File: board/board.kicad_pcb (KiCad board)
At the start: 2 copper layers, 93 x 29 mm, 5 parts, among them J1 022_battery_cells, J2 022_battery_cells, U1 BK-6223-TR, U2 BK-6223-TR

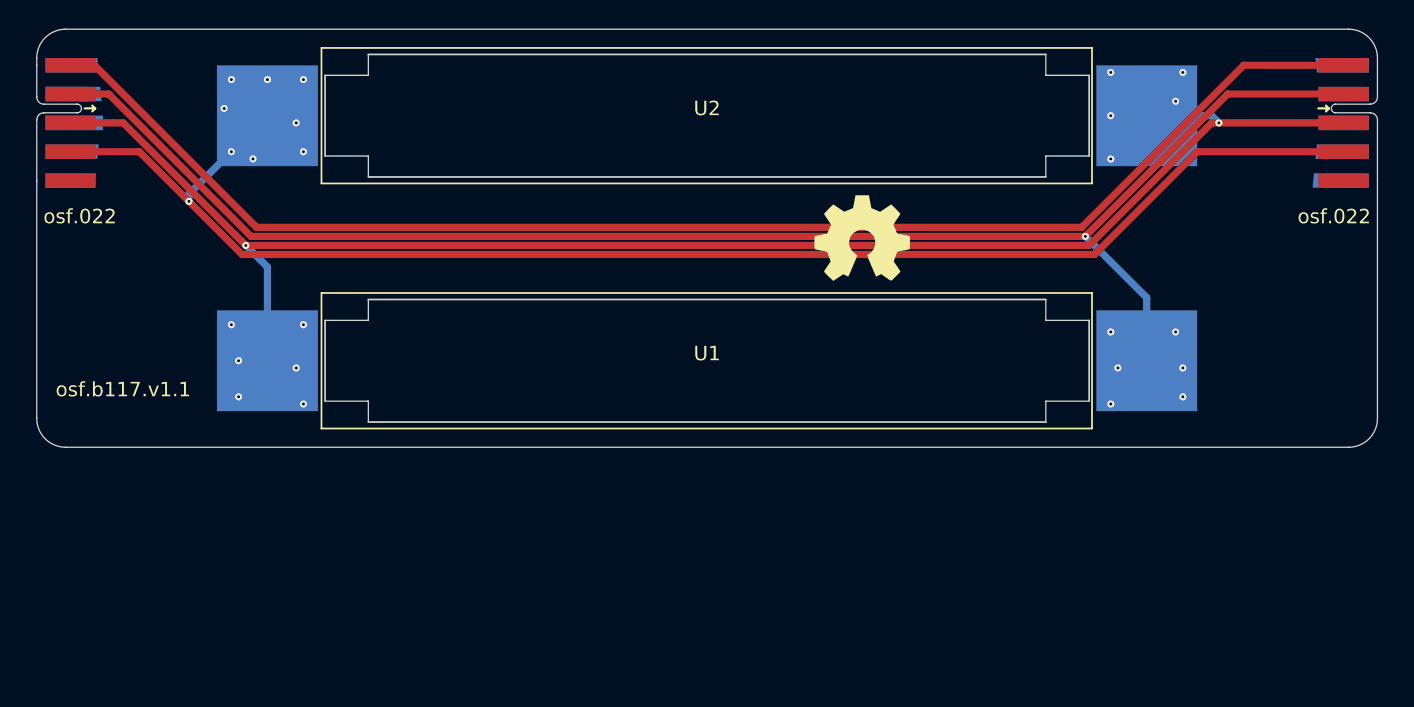
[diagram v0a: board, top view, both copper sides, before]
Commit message: changed to 18650 holder
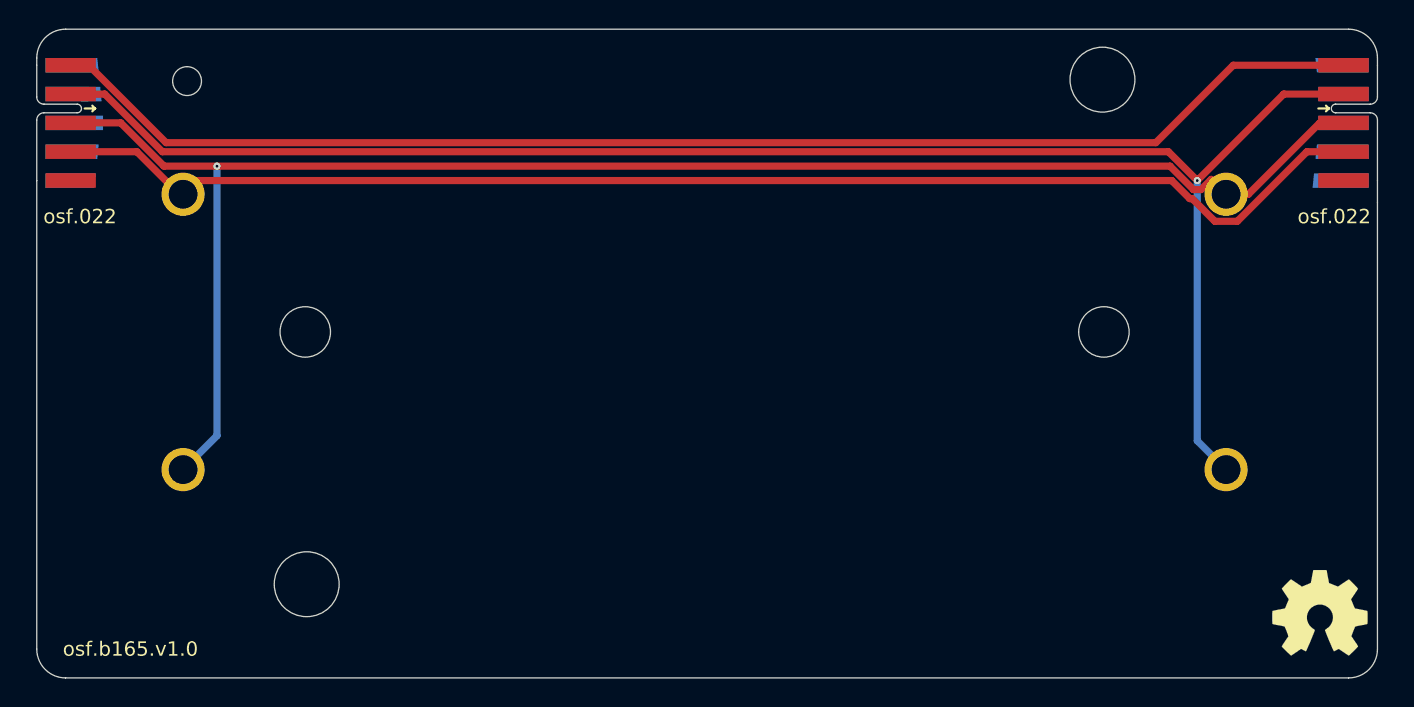
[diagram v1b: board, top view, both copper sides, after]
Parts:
- removed U2: BK-6223-TR, b117:AAA_cell_holder
- U1: value BK-6223-TR -> 2Battery_Cell; footprint b117:AAA_cell_holder -> b165:2_18650_cell_holder
- moved LOGO1 41.0 mm to (217.0, 130.5)
- moved U1 2.01 mm to (174.3, 111.0)
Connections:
- U1 pad 1: /2x_aaa/Low -> /2x_aaa/High
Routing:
- net /2x_aaa/High: track 102.4 -> 93.1 mm, vias 9 -> 0
- net /2x_aaa/Low: track 106.9 -> 114.1 mm, vias 7 -> 1
- net /2x_aaa/Mid: track 109.2 -> 115.0 mm, vias 13 -> 1
- net GND: track 97.6 -> 92.8 mm
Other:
- board size 93 x 29 mm -> 93 x 45 mm
- board text added: "osf.b165.v1.0"
- board text removed: "osf.b117.v1.1"
